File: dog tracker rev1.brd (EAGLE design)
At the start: 54.7 x 35.2 mm, 46 parts, among them IC2 TXB0104, J2 CORTEX_DEBUG_PTH, J6 LiPo, J8 microUSB, Q1 BSS138L, Q2 BSS138L, U2 ATSAMD21G-M, U3 3.3V, X1 LTE-uFL, X2 GNSS-uFL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

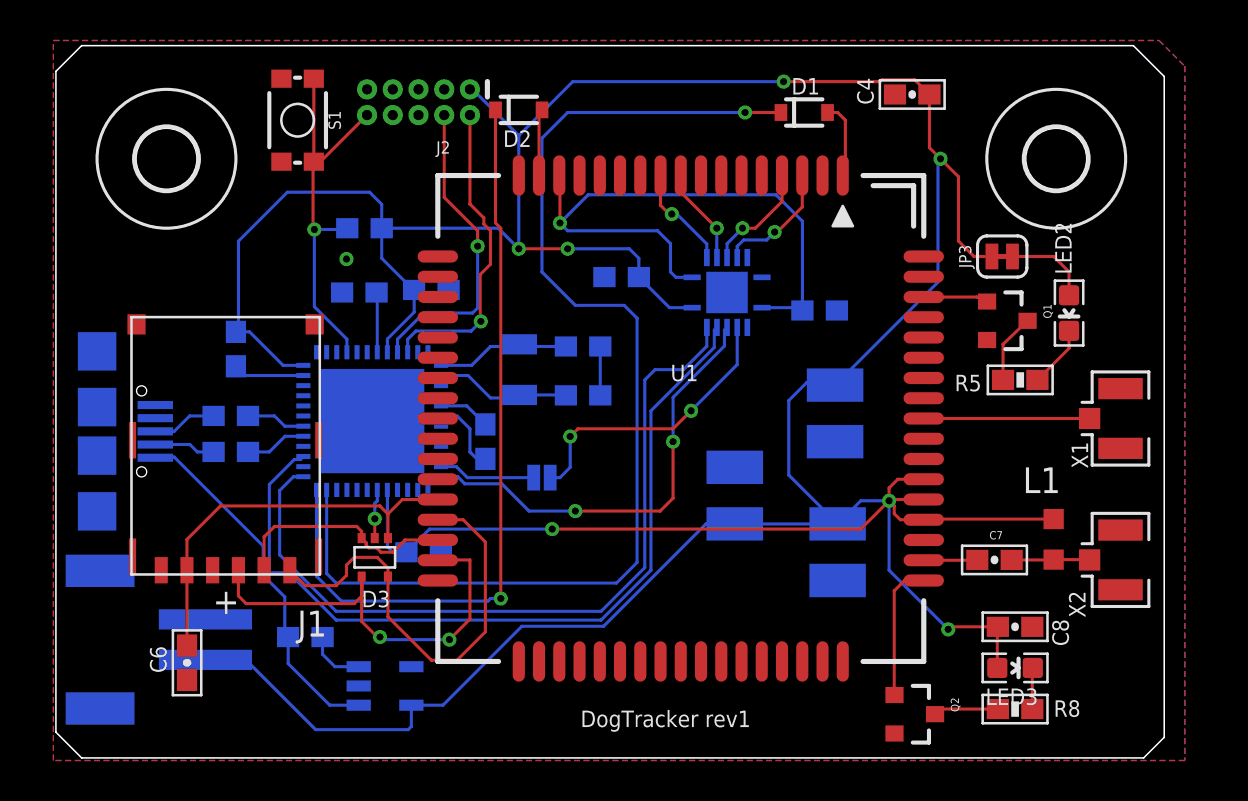
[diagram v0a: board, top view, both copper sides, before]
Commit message: rev1 fixed and sent to fab
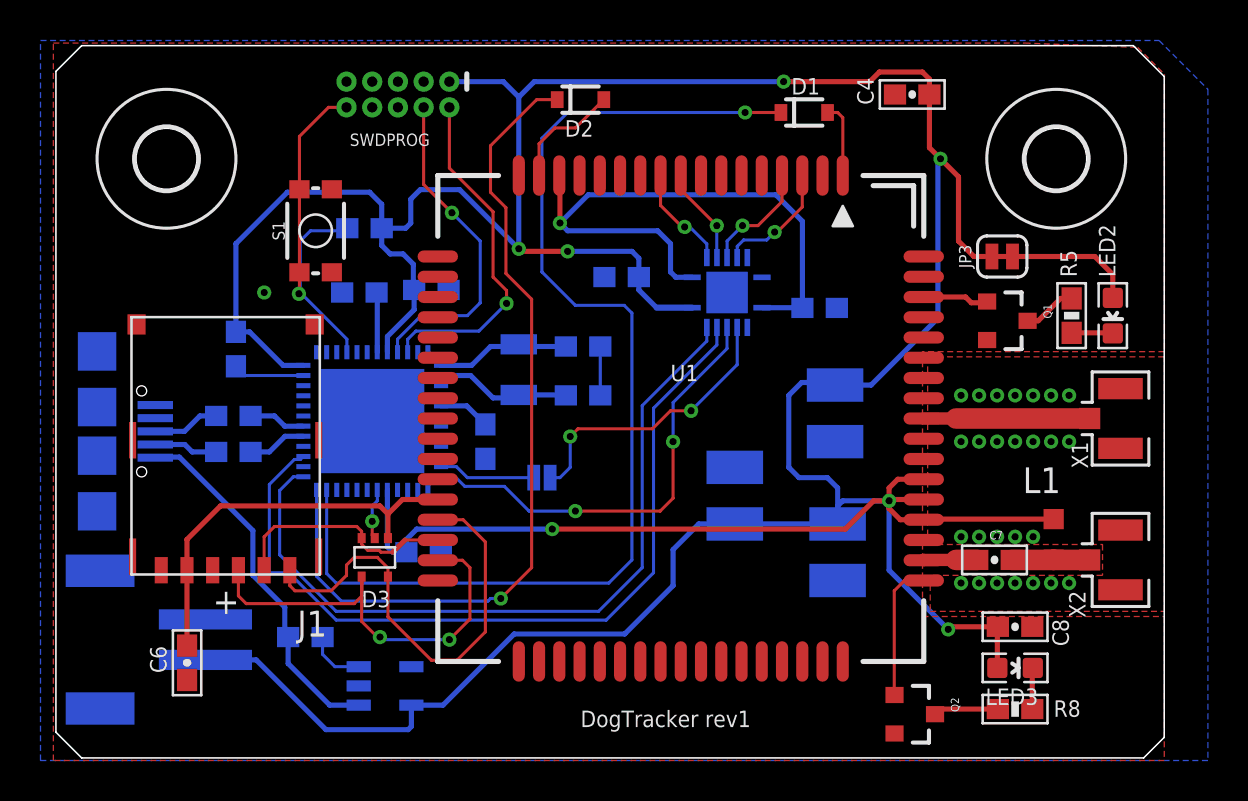
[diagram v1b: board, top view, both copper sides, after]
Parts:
- removed J2: CORTEX_DEBUG_PTH, SparkFun-Connectors:2X5-PTH-1.27MM
- added SWDPROG: CORTEX_DEBUG_PTH, SparkFun-Connectors:2X5-PTH-1.27MM
- moved S1 5.53 mm to (13.0, 26.2), turned to 90 degrees
- moved R5 4.07 mm to (50.3, 22.0), turned to 270 degrees
- moved D2 3.09 mm to (26.0, 32.6)
- moved LED2 2.16 mm to (52.3, 22.0)
- moved R1 0.13 mm to (8.89, 17.0)
- moved R2 0.13 mm to (8.89, 15.2)
- moved C3 0.13 mm to (37.8, 22.4)
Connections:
- net !RESET: now also SWDPROG.10; no longer J2.10
- net 3.3V: now also SWDPROG.1; no longer J2.1
- net GND: now also SWDPROG.3, SWDPROG.5; no longer J2.3, J2.5
- net N$20: now also SWDPROG.7; no longer J2.7
- net N$21: now also SWDPROG.9; no longer J2.9
- net N$24: now also SWDPROG.6; no longer J2.6
- net N$25: now also SWDPROG.8; no longer J2.8
- net SWCLK: now also SWDPROG.4; no longer J2.4
- net SWDIO: now also SWDPROG.2; no longer J2.2
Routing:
- net 3.3V: track 200.9 -> 210.1 mm
- net LTE_RST: track 38.2 -> 42.0 mm
- net VDDANA: track 3.31 -> 0.00 mm
- net NRESET: track 3.30 -> 5.67 mm
- net N$12: track 4.26 -> 6.48 mm
- net SWDIO: track 15.5 -> 17.1 mm
- net SIM_RST: track 22.5 -> 21.3 mm
- net N$5: track 3.07 -> 2.04 mm
- net UC_TXD: track 38.7 -> 37.8 mm
- net SWCLK: track 15.4 -> 16.3 mm
- net N$4: track 3.44 -> 2.63 mm
- net SIM_DATA: track 22.2 -> 22.8 mm
- net GND: track 8.37 -> 8.47 mm, vias 2 -> 28

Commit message: rev1 fixed sim card holder / reset button clearance issue
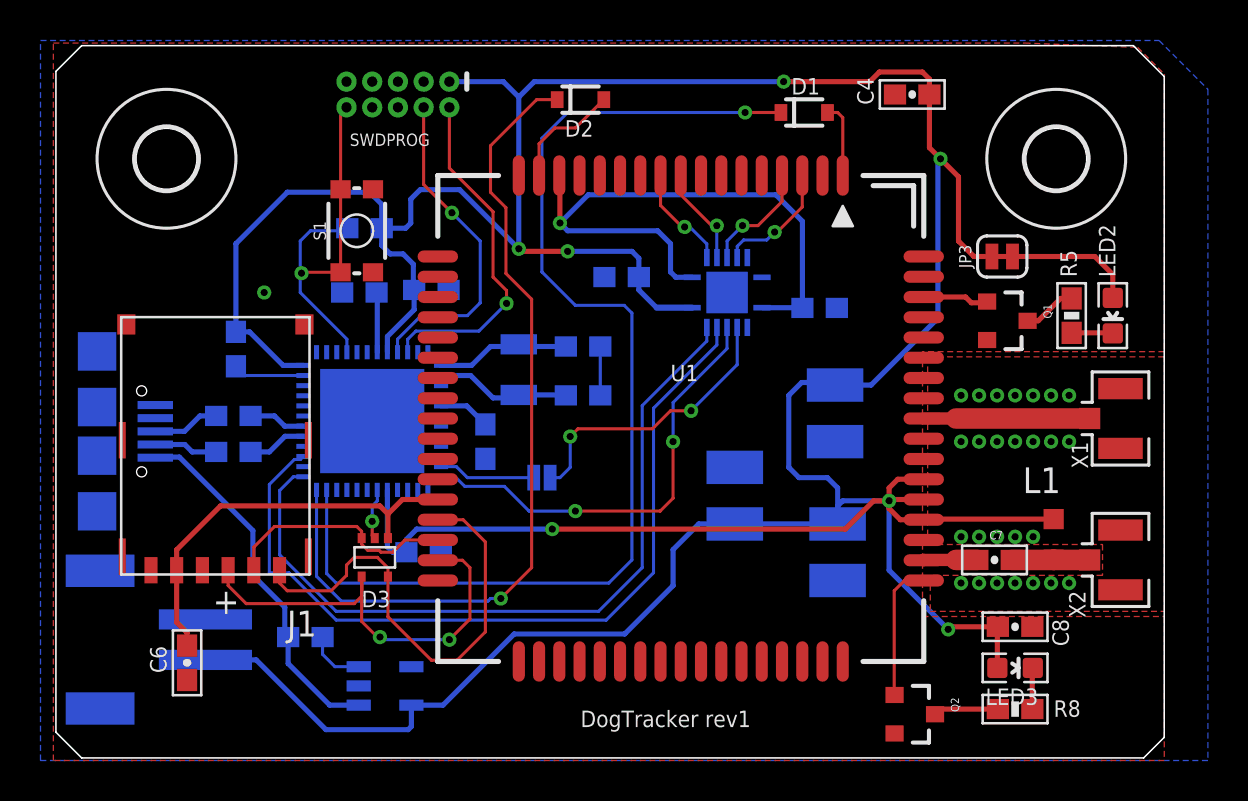
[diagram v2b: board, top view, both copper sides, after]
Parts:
- moved S1 2.03 mm to (15.0, 26.2)
- moved J1 0.51 mm to (8.00, 9.40)
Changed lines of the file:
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@@
 <attribute name="VALUE" x="15.748" y="11.684" size="0.6096" layer="28" font="vector" ratio="20" rot="MR0" align="bottom-center"/>
 </element>
-<element name="J1" library="Wurth_Elektronik_Electromechanic_Input-Output_Connectors_rev16b" package="693043020611" value="" x="8.509" y="9.398" smashed="yes" rot="R180">
-<attribute name="NAME" x="13.509" y="7.398" size="1.27" layer="25" rot="R180"/>
-<attribute name="VALUE" x="13.509" y="24.398" size="1.27" layer="27" rot="R180"/>
+<element name="J1" library="Wurth_Elektronik_Electromechanic_Input-Output_Connectors_rev16b" package="693043020611" value="" x="8.001" y="9.398" smashed="yes" rot="R180">
+<attribute name="NAME" x="13.001" y="7.398" size="1.27" layer="25" rot="R180"/>
+<attribute name="VALUE" x="13.001" y="24.398" size="1.27" layer="27" rot="R180"/>
 </element>
 <element name="Y1" library="SparkFun-Clocks" library_urn="urn:adsk.eagle:library:511" package="CRYSTAL-SMD-3.2X1.5MM" package3d_urn="urn:adsk.eagle:package:37548/1" value="32.768kHz" x="22.987" y="19.304" smashed="yes" rot="MR90">
@@
 <attribute name="POPULARITY" value="3" x="49.53" y="29.718" size="1.778" layer="27" display="off"/>
 </element>
-<element name="S1" library="SparkFun-Switches" library_urn="urn:adsk.eagle:library:535" package="TACTILE_SWITCH_SMD_4.6X2.8MM" package3d_urn="urn:adsk.eagle:package:40176/1" value="Reset" x="12.954" y="26.162" smashed="yes" rot="R90">
-<attribute name="NAME" x="11.43" y="26.162" size="0.6096" layer="25" font="vector" ratio="20" rot="R90" align="bottom-center"/>
-<attribute name="PROD_ID" value="SWCH-13065" x="12.954" y="26.162" size="1.778" layer="27" rot="R90" display="off"/>
-<attribute name="VALUE" x="14.478" y="26.162" size="0.6096" layer="27" font="vector" ratio="20" rot="R90" align="top-center"/>
+<element name="S1" library="SparkFun-Switches" library_urn="urn:adsk.eagle:library:535" package="TACTILE_SWITCH_SMD_4.6X2.8MM" package3d_urn="urn:adsk.eagle:package:40176/1" value="Reset" x="14.986" y="26.162" smashed="yes" rot="R90">
+<attribute name="NAME" x="13.462" y="26.162" size="0.6096" layer="25" font="vector" ratio="20" rot="R90" align="bottom-center"/>
+<attribute name="PROD_ID" value="SWCH-13065" x="14.986" y="26.162" size="1.778" layer="27" rot="R90" display="off"/>
+<attribute name="VALUE" x="16.51" y="26.162" size="0.6096" layer="27" font="vector" ratio="20" rot="R90" align="top-center"/>
 </element>
 <element name="SWDPROG" library="SparkFun-Connectors" library_urn="urn:adsk.eagle:library:513" package="2X5-PTH-1.27MM" package3d_urn="urn:adsk.eagle:package:38290/1" value="CORTEX_DEBUG_PTH" x="17.018" y="32.893" smashed="yes" rot="R180">
@@
 <contactref element="C6" pad="1"/>
 <contactref element="J1" pad="C1"/>
-<wire x1="6.599" y1="9.398" x2="6.599" y2="10.917" width="0.254" layer="1"/>
-<wire x1="6.599" y1="10.917" x2="8.255" y2="12.573" width="0.254" layer="1"/>
+<wire x1="6.091" y1="9.398" x2="6.091" y2="10.409" width="0.254" layer="1"/>
+<wire x1="6.091" y1="10.409" x2="8.255" y2="12.573" width="0.254" layer="1"/>
 <wire x1="8.255" y1="12.573" x2="16.129" y2="12.573" width="0.254" layer="1"/>
 <wire x1="16.525" y1="12.177" x2="16.525" y2="10.983" width="0.254" layer="1"/>
@@
 <wire x1="18.988" y1="12.891" x2="17.239" y2="12.891" width="0.254" layer="1"/>
 <wire x1="17.239" y1="12.891" x2="16.525" y2="12.177" width="0.254" layer="1"/>
-<wire x1="6.604" y1="5.676" x2="6.599" y2="5.681" width="0.1524" layer="1"/>
-<wire x1="6.599" y1="5.681" x2="6.599" y2="9.398" width="0.254" layer="1"/>
+<wire x1="6.604" y1="5.676" x2="6.604" y2="6.311" width="0.254" layer="1"/>
+<wire x1="6.604" y1="6.311" x2="6.091" y2="6.824" width="0.254" layer="1"/>
+<wire x1="6.091" y1="6.824" x2="6.091" y2="9.398" width="0.254" layer="1"/>
 </signal>
 <signal name="SIM_RST">
@@
 <contactref element="D3" pad="4"/>
 <contactref element="J1" pad="C2"/>
-<wire x1="9.139" y1="9.398" x2="9.139" y2="8.133" width="0.1524" layer="1"/>
-<wire x1="9.139" y1="8.133" x2="9.525" y2="7.747" width="0.1524" layer="1"/>
+<wire x1="8.631" y1="9.398" x2="8.631" y2="8.641" width="0.1524" layer="1"/>
+<wire x1="8.631" y1="8.641" x2="9.525" y2="7.747" width="0.1524" layer="1"/>
 <wire x1="14.859" y1="7.747" x2="15.24" y2="8.128" width="0.1524" layer="1"/>
 <wire x1="15.24" y1="8.128" x2="15.24" y2="9.068" width="0.1524" layer="1"/>
@@
 <contactref element="D3" pad="3"/>
 <contactref element="J1" pad="C3"/>
-<wire x1="10.409" y1="9.398" x2="10.409" y2="11.044" width="0.1524" layer="1"/>
-<wire x1="10.409" y1="11.044" x2="10.922" y2="11.557" width="0.1524" layer="1"/>
+<wire x1="9.901" y1="9.398" x2="9.901" y2="10.536" width="0.1524" layer="1"/>
+<wire x1="9.901" y1="10.536" x2="10.922" y2="11.557" width="0.1524" layer="1"/>
 <wire x1="10.922" y1="11.557" x2="14.986" y2="11.557" width="0.1524" layer="1"/>
 <wire x1="14.986" y1="11.557" x2="15.225" y2="11.318" width="0.1524" layer="1"/>
 <wire x1="15.225" y1="11.318" x2="15.225" y2="10.983" width="0.1524" layer="1"/>
 <wire x1="18.988" y1="10.891" x2="17.368" y2="10.891" width="0.1524" layer="1"/>
-<wire x1="17.368" y1="10.891" x2="16.764" y2="10.287" width="0.254" layer="1"/>
+<wire x1="17.368" y1="10.891" x2="16.764" y2="10.287" width="0.1524" layer="1"/>
 <wire x1="16.764" y1="10.287" x2="16.17905625" y2="10.287" width="0.1524" layer="1"/>
 <wire x1="16.08865625" y1="10.3774" x2="16.17905625" y2="10.287" width="0.1524" layer="1"/>
@@
 <contactref element="D3" pad="5"/>
 <contactref element="J1" pad="C7"/>
-<wire x1="11.679" y1="9.398" x2="11.679" y2="8.636" width="0.1524" layer="1"/>
-<wire x1="11.933" y1="8.382" x2="11.679" y2="8.636" width="0.1524" layer="1"/>
-<wire x1="11.933" y1="8.382" x2="13.716" y2="8.382" width="0.1524" layer="1"/>
+<wire x1="11.171" y1="9.398" x2="11.171" y2="8.763" width="0.1524" layer="1"/>
+<wire x1="11.552" y1="8.382" x2="11.171" y2="8.763" width="0.1524" layer="1"/>
+<wire x1="11.552" y1="8.382" x2="13.716" y2="8.382" width="0.1524" layer="1"/>
 <wire x1="13.716" y1="8.382" x2="14.478" y2="9.144" width="0.1524" layer="1"/>
 <wire x1="14.478" y1="9.144" x2="14.478" y2="9.652" width="0.1524" layer="1"/>
@@
 <contactref element="IC2" pad="3"/>
 <contactref element="U1" pad="9"/>
-<wire x1="30.988" y1="28.891" x2="30.988" y2="28.194" width="0.1524" layer="1"/>
-<wire x1="30.988" y1="28.194" x2="32.766" y2="26.416" width="0.1524" layer="1"/>
+<wire x1="30.988" y1="28.891" x2="30.988" y2="27.94" width="0.1524" layer="1"/>
+<wire x1="32.512" y1="26.416" x2="30.988" y2="27.94" width="0.1524" layer="1"/>
+<wire x1="32.512" y1="26.416" x2="32.766" y2="26.416" width="0.1524" layer="1"/>
 <via x="32.766" y="26.416" extent="1-16" drill="0.35"/>
 <wire x1="32.766" y1="26.416" x2="32.766" y2="24.847" width="0.1524" layer="16"/>
@@
 <contactref element="S1" pad="3"/>
 <contactref element="S1" pad="4"/>
-<wire x1="12.154" y1="24.112" x2="12.154" y2="28.212" width="0.1524" layer="1"/>
+<wire x1="14.186" y1="24.112" x2="14.186" y2="28.212" width="0.1524" layer="1"/>
 <wire x1="14.498" y1="20.164" x2="14.498" y2="20.808" width="0.1524" layer="16"/>
 <contactref element="SWDPROG" pad="10"/>
-<via x="12.1285" y="23.0505" extent="1-16" drill="0.35"/>
-<wire x1="12.1285" y1="23.0505" x2="12.154" y2="23.076" width="0.1524" layer="1"/>
-<wire x1="12.154" y1="23.076" x2="12.154" y2="24.112" width="0.1524" layer="1"/>
+<via x="12.2555" y="24.0665" extent="1-16" drill="0.35"/>
+<wire x1="12.2555" y1="24.0665" x2="12.301" y2="24.112" width="0.1524" layer="1"/>
+<wire x1="12.301" y1="24.112" x2="14.186" y2="24.112" width="0.1524" layer="1"/>
 <wire x1="14.498" y1="20.808" x2="12.192" y2="23.114" width="0.1524" layer="16"/>
-<wire x1="12.154" y1="28.212" x2="12.154" y2="30.823" width="0.1524" layer="1"/>
-<wire x1="12.154" y1="30.823" x2="13.589" y2="32.258" width="0.1524" layer="1"/>
-<wire x1="13.589" y1="32.258" x2="14.478" y2="32.258" width="0.1524" layer="1"/>
+<wire x1="14.186" y1="28.212" x2="14.186" y2="32.258" width="0.1524" layer="1"/>
+<wire x1="14.186" y1="32.258" x2="14.478" y2="32.258" width="0.1524" layer="1"/>
 <wire x1="14.39" y1="26.162" x2="12.7" y2="26.162" width="0.1524" layer="16"/>
 <wire x1="12.7" y1="26.162" x2="12.192" y2="25.654" width="0.1524" layer="16"/>
-<wire x1="12.192" y1="23.114" x2="12.1285" y2="23.0505" width="0.1524" layer="16"/>
+<wire x1="12.192" y1="24.003" x2="12.2555" y2="24.0665" width="0.1524" layer="16"/>
 <wire x1="14.517" y1="26.289" x2="14.39" y2="26.162" width="0.1524" layer="16"/>
-<wire x1="12.192" y1="25.654" x2="12.192" y2="23.114" width="0.1524" layer="16"/>
+<wire x1="12.192" y1="25.654" x2="12.192" y2="24.003" width="0.1524" layer="16"/>
+<wire x1="12.192" y1="24.003" x2="12.192" y2="23.114" width="0.1524" layer="16"/>
 </signal>
 <signal name="3.3V">

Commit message: rev1 resolved other minor issues, added battery sense, routed all power through LDO and added diode mixing to power input.
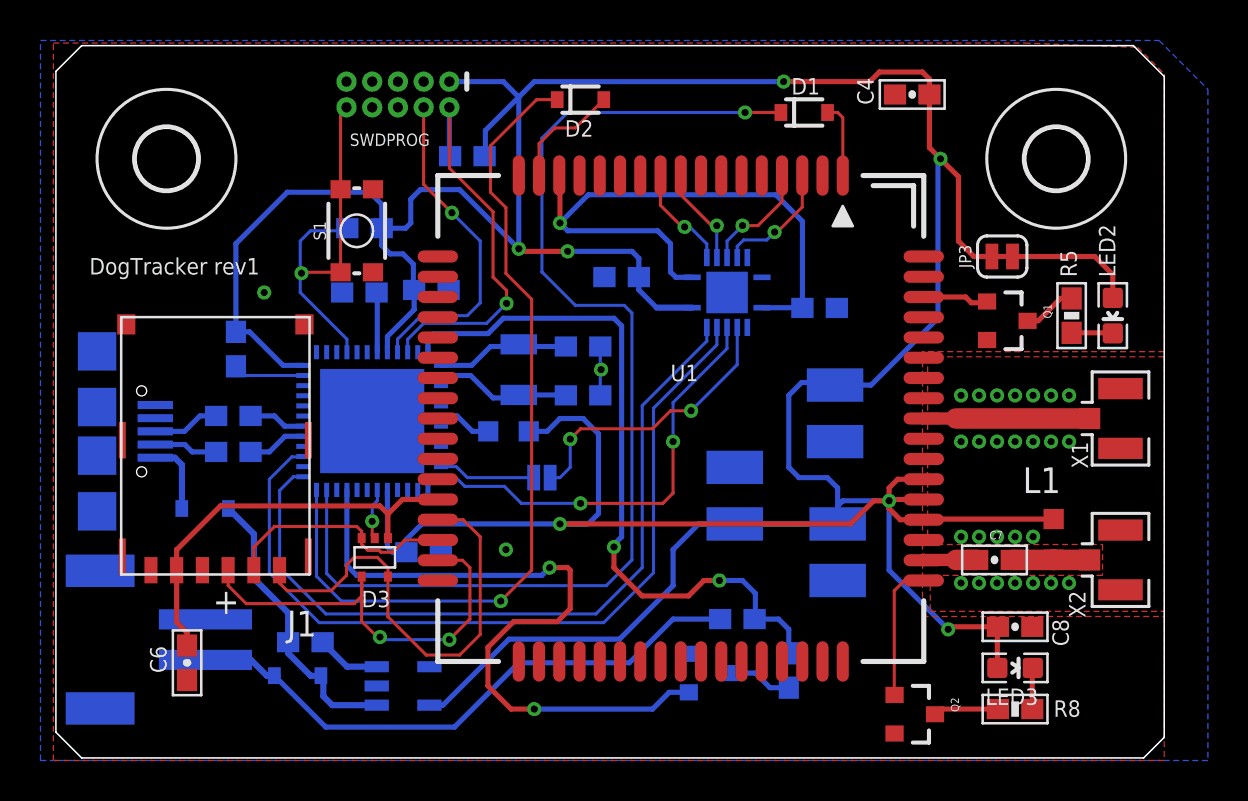
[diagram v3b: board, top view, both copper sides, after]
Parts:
- removed C5: 0.1uF, TimWoo-Capacitors:0603-CAP-MARKED
- added D4, D5: 1A/23V/620mV, SparkFun-DiscreteSemi:SOD-323
- added L2: 27nh, rcl:L2012C
- added Q3: BSS138L, TimWoo-MOSFETs:SOT23-3
- added R6: 30k, TimWoo-Resistors:0603-RES-MARKED
- added R7, R9: 10k, TimWoo-Resistors:0603-RES-MARKED
- moved U3 0.89 mm to (17.3, 3.68)
- moved R4 0.25 mm to (12.4, 5.84)
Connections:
- removed net N$14: C5.2, U2.5
- removed net N$21: SWDPROG.9
- new net BATT_SENSE: R6.2, R7.1, U2.48
- new net N$15: Q3.3, R6.1
- new net N$19: D4.C, D5.C, R4.1, U3.1
- new net SENSE_GATE: Q3.1, U2.21
- new net V_BATT: D5.A, J6.2, R7.2
- net 3.3V: now also L2.1, R9.2; no longer J6.2
- net GND: now also Q3.2, SWDPROG.9, U2.5; no longer C5.1
- net SWDIO: now also R9.1
- net VDDANA: now also L2.2
- net V_USB: now also D4.A; no longer R4.1, U3.1
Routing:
- net BATT_SENSE: track 0.00 -> 35.4 mm, vias 0 -> 2
- net SENSE_GATE: track 0.00 -> 34.6 mm, vias 0 -> 2
- net V_BATT: track 0.00 -> 29.3 mm
- net N$19: track 0.00 -> 14.4 mm
- net V_USB: track 18.0 -> 3.67 mm
- net N$15: track 0.00 -> 3.24 mm
- net VDDANA: track 0.00 -> 2.64 mm
- net N$14: track 2.57 -> 0.00 mm
- net SWDIO: track 17.1 -> 19.5 mm
- net GND: vias 28 -> 30

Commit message: rev1.1
fixed USB and serial connections
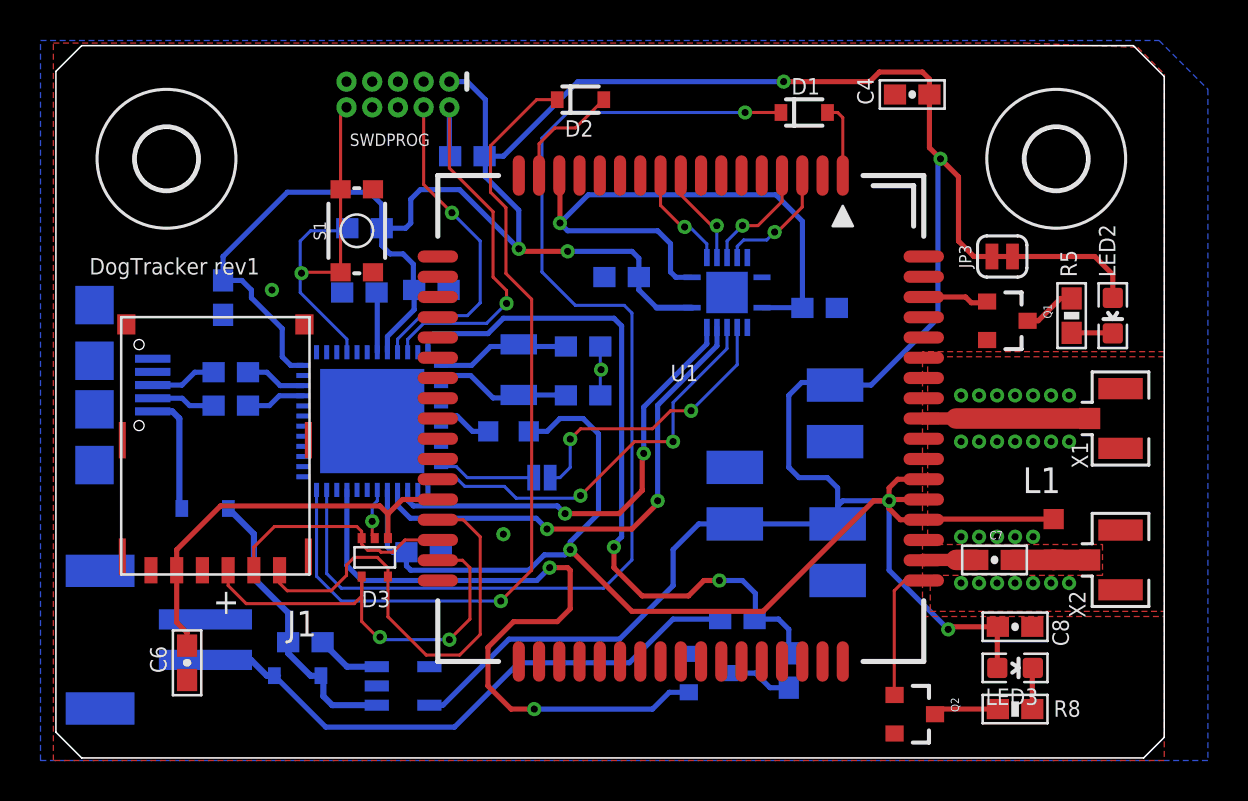
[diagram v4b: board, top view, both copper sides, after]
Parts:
- moved C16 2.62 mm to (8.38, 22.9)
- moved J8 2.29 mm to (2.03, 18.5)
- moved R2 2.29 mm to (8.76, 17.5)
- moved R1 2.16 mm to (8.76, 19.2)
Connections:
- net N$13: now also R1.2, U2.34; no longer R2.2, U2.29
- net N$9: now also R2.2, U2.33; no longer R1.2, U2.30
- net UC_RXD: now also U2.16; no longer U2.27
- net UC_TXD: now also U2.15; no longer U2.25
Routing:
- net UC_RXD: track 41.2 -> 24.5 mm, vias 0 -> 2
- net UC_TXD: track 38.2 -> 22.2 mm, vias 0 -> 2
- net GND: track 8.47 -> 4.95 mm
- net 3.3V: track 210.2 -> 213.0 mm
- net V_USB: track 3.67 -> 6.00 mm
- net UC_RI: track 21.5 -> 19.8 mm
